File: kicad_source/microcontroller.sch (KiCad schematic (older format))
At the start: 47 parts, among them CN1 Micro_SDCard, CN2 CONN_02X05, CN5 CONN_01X14, CN6 CONN_01X04, SW1 TAST_VER, SW2 TAST_VER, SW3 SW_PUSH, SW4 TAST_VER, U1 W25Q80D, U2 ATECC608A, U3 FE310-G002, U8 BMA400, Y1 16MHz

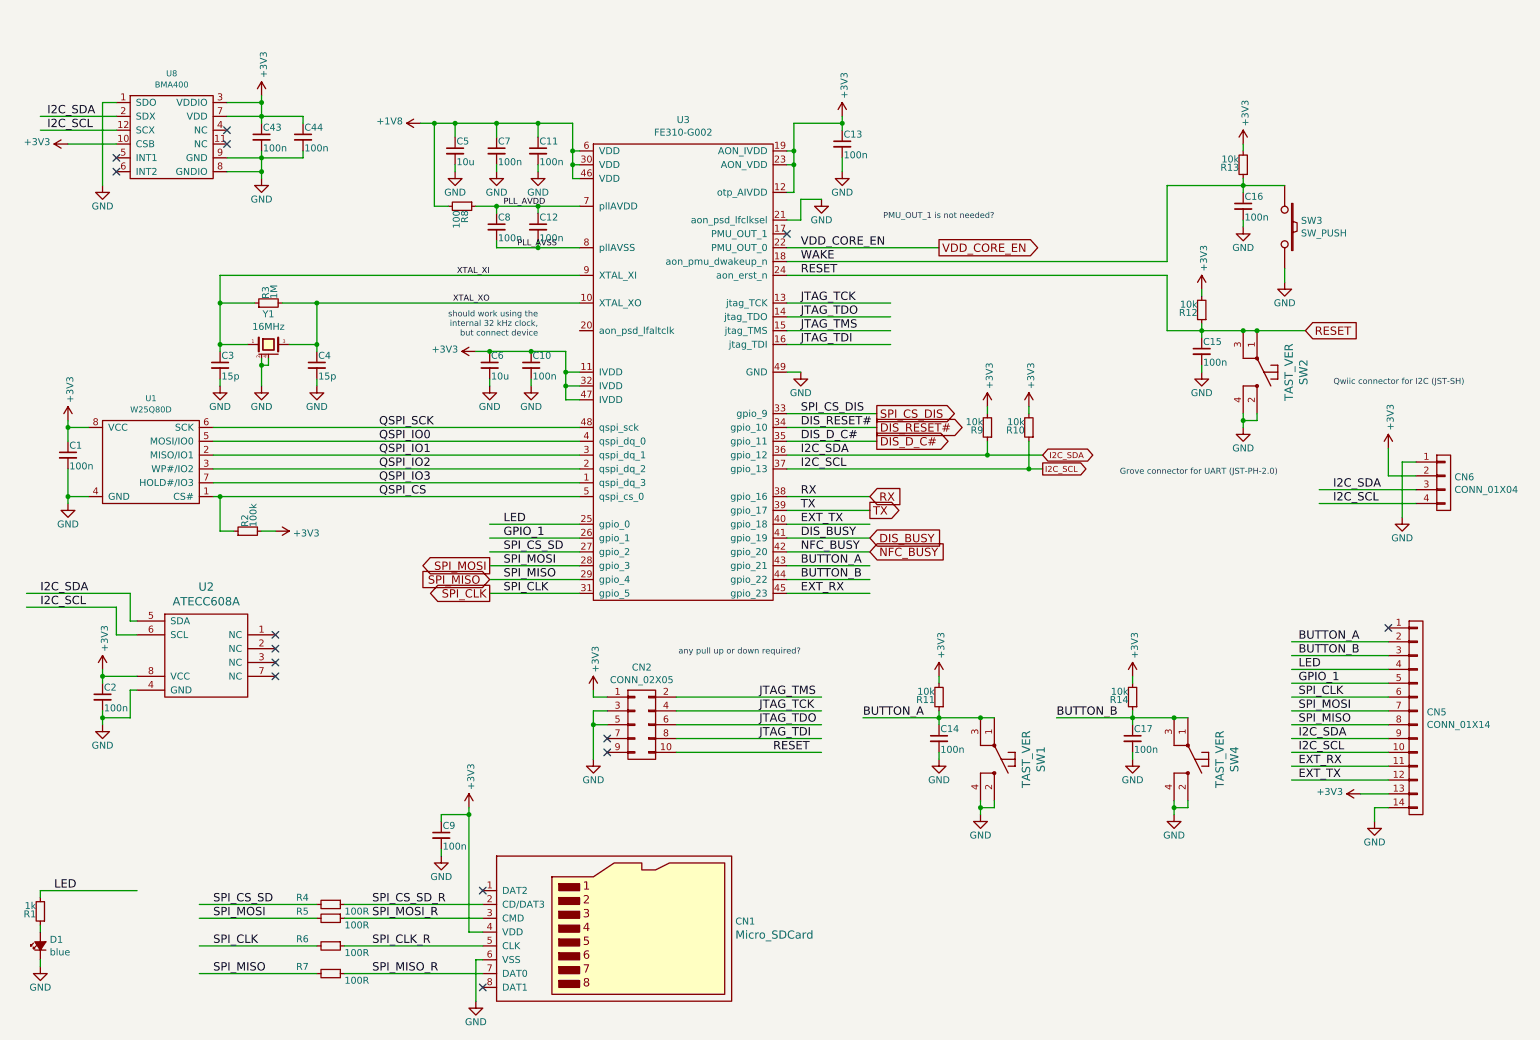
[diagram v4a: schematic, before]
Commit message: corrected some part numbers
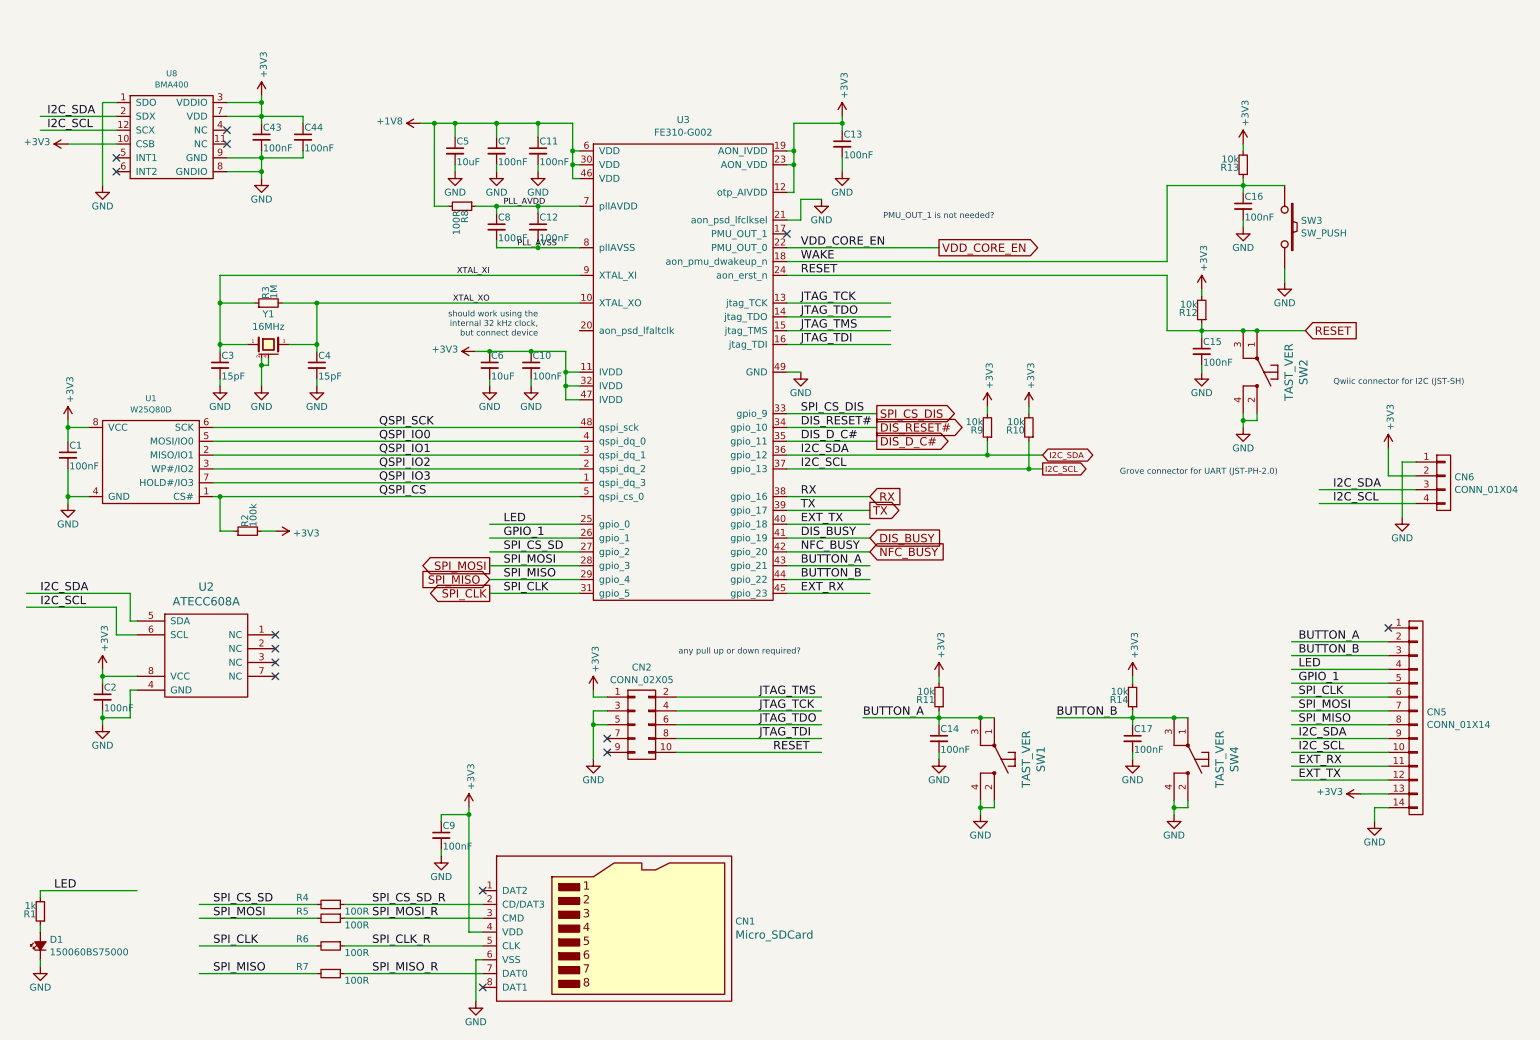
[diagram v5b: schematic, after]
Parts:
- C1, C10, C11, C12, C13, C14, C15, C16, C17, C2, C43, C44, C7, C8, C9: value 100n -> 100nF
- C3, C4: value 15p -> 15pF
- C5, C6: value 10u -> 10uF
- D1: value blue -> 150060BS75000
- R8: value 100 -> 100R
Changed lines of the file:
@@
 P 4250 2950
 F 0 "C10" H 4260 3020 50  0000 L CNN
-F 1 "100n" H 4260 2870 50  0000 L CNN
+F 1 "100nF" H 4260 2870 50  0000 L CNN
 F 2 "capacitors:C_0603" H 4250 2800 50  0001 C CNN
 F 3 "" H 4250 2950 50  0000 C CNN
@@
 P 3950 2950
 F 0 "C6" H 3960 3020 50  0000 L CNN
-F 1 "10u" H 3960 2870 50  0000 L CNN
+F 1 "10uF" H 3960 2870 50  0000 L CNN
 F 2 "capacitors:C_0603" H 3950 2800 50  0001 C CNN
 F 3 "" H 3950 2950 50  0000 C CNN
@@
 P 9100 2850
 F 0 "C15" H 9110 2920 50  0000 L CNN
-F 1 "100n" H 9110 2770 50  0000 L CNN
+F 1 "100nF" H 9110 2770 50  0000 L CNN
 F 2 "capacitors:C_0603" H 9100 2700 50  0001 C CNN
 F 3 "" H 9100 2850 50  0000 C CNN
@@
 P 3600 6350
 F 0 "C9" H 3610 6420 50  0000 L CNN
-F 1 "100n" H 3610 6270 50  0000 L CNN
+F 1 "100nF" H 3610 6270 50  0000 L CNN
 F 2 "capacitors:C_0603" H 3600 6200 50  0001 C CNN
 F 3 "" H 3600 6350 50  0000 C CNN
@@
 P 700 7150
 F 0 "D1" V 746 7082 50  0000 R CNN
-F 1 "blue" V 655 7082 50  0000 R CNN
+F 1 "150060BS75000" V 655 7082 50  0000 R CNN
 F 2 "LEDs:LED_0603" V 700 7150 50  0001 C CNN
 F 3 "" V 700 7150 50  0000 C CNN
@@
 P 1150 5350
 F 0 "C2" H 1160 5420 50  0000 L CNN
-F 1 "100n" H 1160 5270 50  0000 L CNN
+F 1 "100nF" H 1160 5270 50  0000 L CNN
 F 2 "capacitors:C_0603" H 1150 5200 50  0001 C CNN
 F 3 "" H 1150 5350 50  0000 C CNN
@@
 P 4300 1950
 F 0 "C12" H 4310 2020 50  0000 L CNN
-F 1 "100n" H 4310 1870 50  0000 L CNN
+F 1 "100nF" H 4310 1870 50  0000 L CNN
 F 2 "capacitors:C_0603" H 4300 1800 50  0001 C CNN
 F 3 "" H 4300 1950 50  0000 C CNN
@@
 P 4000 1950
 F 0 "C8" H 4010 2020 50  0000 L CNN
-F 1 "100n" H 4010 1870 50  0000 L CNN
+F 1 "100nF" H 4010 1870 50  0000 L CNN
 F 2 "capacitors:C_0603" H 4000 1800 50  0001 C CNN
 F 3 "" H 4000 1950 50  0000 C CNN
@@
 P 4300 1400
 F 0 "C11" H 4310 1470 50  0000 L CNN
-F 1 "100n" H 4310 1320 50  0000 L CNN
+F 1 "100nF" H 4310 1320 50  0000 L CNN
 F 2 "capacitors:C_0603" H 4300 1250 50  0001 C CNN
 F 3 "" H 4300 1400 50  0000 C CNN
@@
 P 4000 1400
 F 0 "C7" H 4010 1470 50  0000 L CNN
-F 1 "100n" H 4010 1320 50  0000 L CNN
+F 1 "100nF" H 4010 1320 50  0000 L CNN
 F 2 "capacitors:C_0603" H 4000 1250 50  0001 C CNN
 F 3 "" H 4000 1400 50  0000 C CNN
@@
 P 3700 1400
 F 0 "C5" H 3710 1470 50  0000 L CNN
-F 1 "10u" H 3710 1320 50  0000 L CNN
+F 1 "10uF" H 3710 1320 50  0000 L CNN
 F 2 "capacitors:C_0603" H 3700 1250 50  0001 C CNN
 F 3 "" H 3700 1400 50  0000 C CNN
@@
 P 3750 1800
 F 0 "R8" H 3780 1820 50  0000 L CNN
-F 1 "100" H 3780 1760 50  0000 L CNN
+F 1 "100R" H 3780 1760 50  0000 L CNN
 F 2 "resistors:R_0603" H 3750 1650 50  0001 C CNN
 F 3 "" H 3750 1800 50  0000 C CNN
@@
 P 6500 1350
 F 0 "C13" H 6510 1420 50  0000 L CNN
-F 1 "100n" H 6510 1270 50  0000 L CNN
+F 1 "100nF" H 6510 1270 50  0000 L CNN
 F 2 "capacitors:C_0603" H 6500 1200 50  0001 C CNN
 F 3 "" H 6500 1350 50  0000 C CNN
@@
 P 9400 1800
 F 0 "C16" H 9410 1870 50  0000 L CNN
-F 1 "100n" H 9410 1720 50  0000 L CNN
+F 1 "100nF" H 9410 1720 50  0000 L CNN
 F 2 "capacitors:C_0603" H 9400 1650 50  0001 C CNN
 F 3 "" H 9400 1800 50  0000 C CNN
@@
 P 2000 2950
 F 0 "C3" H 2010 3020 50  0000 L CNN
-F 1 "15p" H 2010 2870 50  0000 L CNN
+F 1 "15pF" H 2010 2870 50  0000 L CNN
 F 2 "capacitors:C_0603" H 2000 2800 50  0001 C CNN
 F 3 "" H 2000 2950 50  0000 C CNN
@@
 P 2700 2950
 F 0 "C4" H 2710 3020 50  0000 L CNN
-F 1 "15p" H 2710 2870 50  0000 L CNN
+F 1 "15pF" H 2710 2870 50  0000 L CNN
 F 2 "capacitors:C_0603" H 2700 2800 50  0001 C CNN
 F 3 "" H 2700 2950 50  0000 C CNN
@@
 P 900 3600
 F 0 "C1" H 910 3670 50  0000 L CNN
-F 1 "100n" H 910 3520 50  0000 L CNN
+F 1 "100nF" H 910 3520 50  0000 L CNN
 F 2 "capacitors:C_0603" H 900 3450 50  0001 C CNN
 F 3 "" H 900 3600 50  0000 C CNN
@@
 P 7200 5650
 F 0 "C14" H 7210 5720 50  0000 L CNN
-F 1 "100n" H 7210 5570 50  0000 L CNN
+F 1 "100nF" H 7210 5570 50  0000 L CNN
 F 2 "capacitors:C_0603" H 7200 5500 50  0001 C CNN
 F 3 "" H 7200 5650 50  0000 C CNN
@@
 P 8600 5650
 F 0 "C17" H 8610 5720 50  0000 L CNN
-F 1 "100n" H 8610 5570 50  0000 L CNN
+F 1 "100nF" H 8610 5570 50  0000 L CNN
 F 2 "capacitors:C_0603" H 8600 5500 50  0001 C CNN
 F 3 "" H 8600 5650 50  0000 C CNN
@@
 P 2300 1300
 F 0 "C43" H 2310 1370 50  0000 L CNN
-F 1 "100n" H 2310 1220 50  0000 L CNN
+F 1 "100nF" H 2310 1220 50  0000 L CNN
 F 2 "capacitors:C_0603" H 2300 1150 50  0001 C CNN
 F 3 "" H 2300 1300 50  0000 C CNN
@@
 P 2600 1300
 F 0 "C44" H 2610 1370 50  0000 L CNN
-F 1 "100n" H 2610 1220 50  0000 L CNN
+F 1 "100nF" H 2610 1220 50  0000 L CNN
 F 2 "capacitors:C_0603" H 2600 1150 50  0001 C CNN
 F 3 "" H 2600 1300 50  0000 C CNN

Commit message: added some missing part numbers
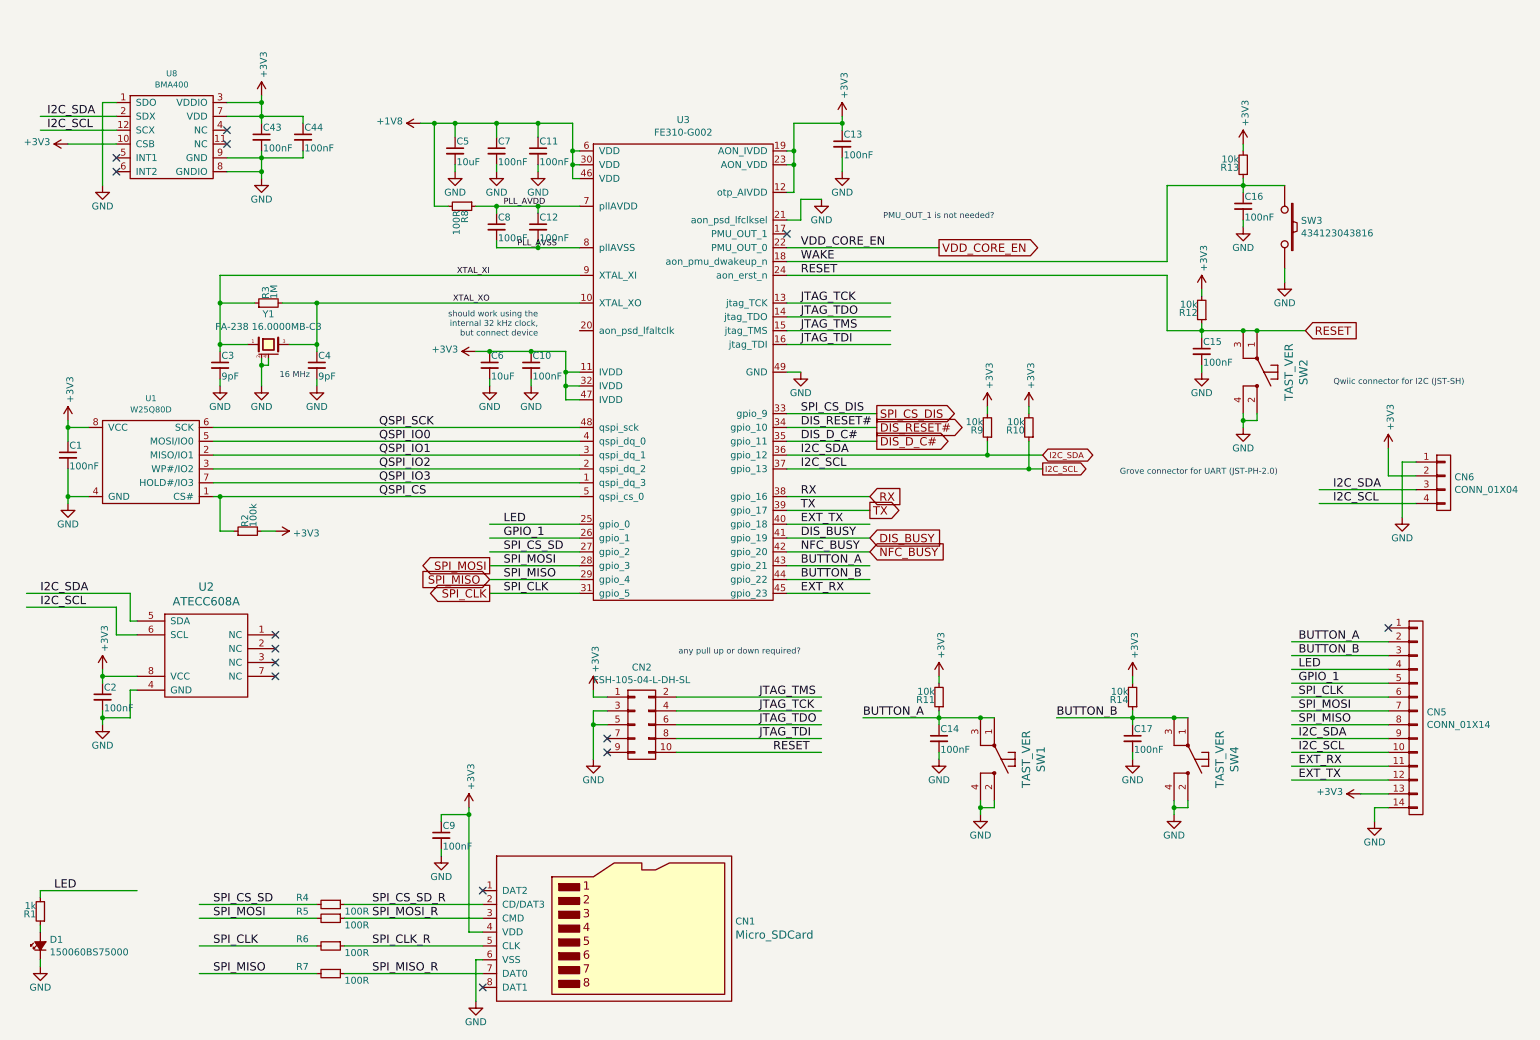
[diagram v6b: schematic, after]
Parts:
- C3, C4: value 15pF -> 9pF
- CN2: value CONN_02X05 -> FSH-105-04-L-DH-SL
- SW3: value SW_PUSH -> 434123043816
- Y1: value 16MHz -> FA-238 16.0000MB-C3
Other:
- note added: "16 MHz"
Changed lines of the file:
@@
 P 2350 2800
 F 0 "Y1" H 2350 3020 50  0000 C CNN
-F 1 "16MHz" H 2350 2929 50  0000 C CNN
+F 1 "FA-238 16.0000MB-C3" H 2350 2929 50  0000 C CNN
 F 2 "crystals:Crystal_SMD_3.2x2.5mm_4Pad" H 2350 2600 50  0001 C CNN
 F 3 "" H 2350 2800 50  0000 C CNN
@@
 P 2000 2950
 F 0 "C3" H 2010 3020 50  0000 L CNN
-F 1 "15pF" H 2010 2870 50  0000 L CNN
+F 1 "9pF" H 2010 2870 50  0000 L CNN
 F 2 "capacitors:C_0603" H 2000 2800 50  0001 C CNN
 F 3 "" H 2000 2950 50  0000 C CNN
@@
 P 2700 2950
 F 0 "C4" H 2710 3020 50  0000 L CNN
-F 1 "15pF" H 2710 2870 50  0000 L CNN
+F 1 "9pF" H 2710 2870 50  0000 L CNN
 F 2 "capacitors:C_0603" H 2700 2800 50  0001 C CNN
 F 3 "" H 2700 2950 50  0000 C CNN
@@
 P 5050 5550
 F 0 "CN2" H 5050 5965 50  0000 C CNN
-F 1 "CONN_02X05" H 5050 5874 50  0000 C CNN
+F 1 "FSH-105-04-L-DH-SL" H 5050 5874 50  0000 C CNN
 F 2 "CON_samtec:FSH-105-04-L-DH-SL" H 5050 5550 50  0001 C CNN
 F 3 "" H 5050 4350 50  0000 C CNN
@@
 P 9700 1950
 F 0 "SW3" V 9654 2068 50  0000 L CNN
-F 1 "SW_PUSH" V 9745 2068 50  0000 L CNN
+F 1 "434123043816" V 9745 2068 50  0000 L CNN
 F 2 "mechanical-switches:smd_push" V 9791 2068 50  0001 L CNN
 F 3 "" H 9700 1950 50  0000 C CNN
@@
 Wire Wire Line
 	9700 2250 9700 2350
+Text Notes 2650 3050 2    43   ~ 0
+16 MHz
 $EndSCHEMATC

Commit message: changed BMA400 to BMA253, changed SD-Card-Socket to MEM2061-01-188-00-A and changed battery holder to BAT-HLD-001 for cost reduction
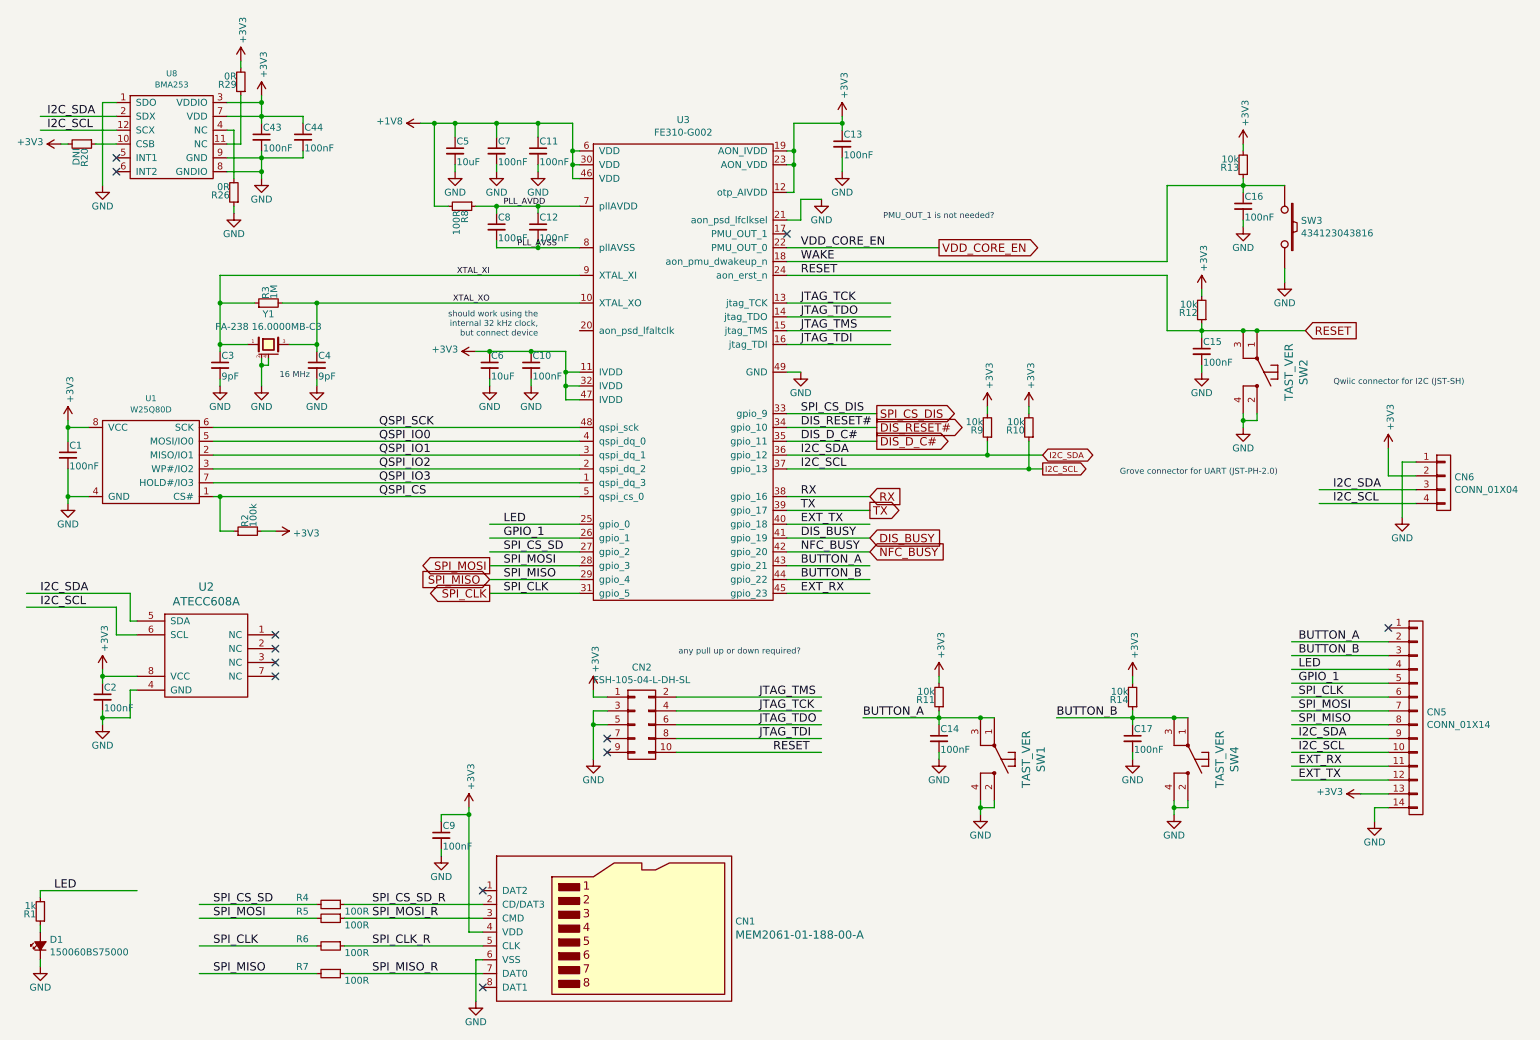
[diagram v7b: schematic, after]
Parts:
- added R20: DNI, resistors:R_0603, symbol devices:R_1206
- added R26, R29: 0R, resistors:R_0603, symbol devices:R_1206
- CN1: value Micro_SDCard -> MEM2061-01-188-00-A
- U8: value BMA400 -> BMA253
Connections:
- wire segments 245 -> 252
- no-connect marks 14 -> 12
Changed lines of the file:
@@
 P 4550 7150
 F 0 "CN1" H 5727 7328 50  0000 L CNN
-F 1 "Micro_SDCard" H 5727 7230 59  0000 L CNN
+F 1 "MEM2061-01-188-00-A" H 5727 7230 59  0000 L CNN
 F 2 "CON_wuerth:WE_693071010811" H 4950 7500 50  0001 C CNN
 F 3 "" H 4750 7150 60  0000 C CNN
@@
 P 1650 1300
 F 0 "U8" H 1650 1760 43  0000 C CNN
-F 1 "BMA400" H 1650 1679 43  0000 C CNN
+F 1 "BMA253" H 1650 1679 43  0000 C CNN
 F 2 "IC_sensor:BMA400" H 1650 1300 43  0001 C CNN
 F 3 "" H 1650 1300 43  0001 C CNN
@@
 Wire Wire Line
 	2300 1150 2300 1050
-NoConn ~ 2050 1250
-NoConn ~ 2050 1350
 NoConn ~ 1250 1450
 NoConn ~ 1250 1550
@@
 L power-supply:+3V3 #PWR091
 U 1 1 5EC8591C
-P 900 1350
-F 0 "#PWR091" H 900 1200 50  0001 C CNN
-F 1 "+3V3" V 915 1478 50  0000 L CNN
-F 2 "" H 900 1350 50  0000 C CNN
-F 3 "" H 900 1350 50  0000 C CNN
-	1    900  1350
+P 850 1350
+F 0 "#PWR091" H 850 1200 50  0001 C CNN
+F 1 "+3V3" V 865 1478 50  0000 L CNN
+F 2 "" H 850 1350 50  0000 C CNN
+F 3 "" H 850 1350 50  0000 C CNN
+	1    850  1350
 	0    -1   -1   0
 $EndComp
-Wire Wire Line
-	1250 1350 900  1350
 Wire Wire Line
 	700  1250 1250 1250
@@
 Text Notes 2650 3050 2    43   ~ 0
 16 MHz
+$Comp
+L devices:R_1206 R26
+U 1 1 5EE7D636
+P 2100 1700
+F 0 "R26" H 2130 1720 50  0000 L CNN
+F 1 "0R" H 2130 1660 50  0000 L CNN
+F 2 "resistors:R_0603" H 2100 1550 50  0001 C CNN
+F 3 "" H 2100 1700 50  0000 C CNN
+	1    2100 1700
+	-1   0    0    1
+$EndComp
+$Comp
+L power-supply:GND #PWR095
+U 1 1 5EE7E688
+P 2100 1850
+F 0 "#PWR095" H 2100 1600 50  0001 C CNN
+F 1 "GND" H 2100 1700 50  0000 C CNN
+F 2 "" H 2100 1850 50  0000 C CNN
+F 3 "" H 2100 1850 50  0000 C CNN
+	1    2100 1850
+	1    0    0    -1
+$EndComp
+Wire Wire Line
+	2050 1250 2100 1250
+Wire Wire Line
+	2100 1250 2100 1600
+Wire Wire Line
+	2100 1800 2100 1850
+$Comp
+L devices:R_1206 R20
+U 1 1 5EEA4316
+P 1000 1350
+F 0 "R20" H 1030 1370 50  0000 L CNN
+F 1 "DNI" H 1030 1310 50  0000 L CNN
+F 2 "resistors:R_0603" H 1000 1200 50  0001 C CNN
+F 3 "" H 1000 1350 50  0000 C CNN
+	1    1000 1350
+	0    1    1    0
+$EndComp
+Wire Wire Line
+	1250 1350 1100 1350
+Wire Wire Line
+	900  1350 850  1350
+$Comp
+L devices:R_1206 R29
+U 1 1 5EEC615E
+P 2150 900
+F 0 "R29" H 2180 920 50  0000 L CNN
+F 1 "0R" H 2180 860 50  0000 L CNN
+F 2 "resistors:R_0603" H 2150 750 50  0001 C CNN
+F 3 "" H 2150 900 50  0000 C CNN
+	1    2150 900
+	-1   0    0    1
+$EndComp
+$Comp
+L power-supply:+3V3 #PWR096
+U 1 1 5EEC652C
+P 2150 750
+F 0 "#PWR096" H 2150 600 50  0001 C CNN
+F 1 "+3V3" V 2165 878 50  0000 L CNN
+F 2 "" H 2150 750 50  0000 C CNN
+F 3 "" H 2150 750 50  0000 C CNN
+	1    2150 750
+	1    0    0    -1
+$EndComp
+Wire Wire Line
+	2050 1350 2150 1350
+Wire Wire Line
+	2150 1350 2150 1000
+Wire Wire Line
+	2150 800  2150 750
 $EndSCHEMATC
